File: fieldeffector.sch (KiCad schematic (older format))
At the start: 30 parts, among them J1 Conn_01x02, J10 Conn_01x02, J2 Conn_01x02, J3 Conn_01x02, J4 Conn_01x02, J5 Conn_01x02, J6 Conn_01x02, J7 Conn_01x02, J8 Conn_01x02, J9 Conn_01x02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

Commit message: update layout
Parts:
- added H1, H2, H3, H4: MountingHole, MountingHole:MountingHole_3.2mm_M3, symbol Mechanical:MountingHole
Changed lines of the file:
@@
 EESchema Schematic File Version 4
-LIBS:fieldeffect4-cache
+LIBS:fieldeffector-cache
 EELAYER 26 0
 EELAYER END
@@
 Wire Wire Line
 	7000 3000 7000 3050
+$Comp
+L Mechanical:MountingHole H3
+U 1 1 5CB01E0B
+P 1800 3400
+F 0 "H3" H 1900 3446 50  0000 L CNN
+F 1 "MountingHole" H 1900 3355 50  0000 L CNN
+F 2 "MountingHole:MountingHole_3.2mm_M3" H 1800 3400 50  0001 C CNN
+F 3 "~" H 1800 3400 50  0001 C CNN
+	1    1800 3400
+	1    0    0    -1
+$EndComp
+$Comp
+L Mechanical:MountingHole H4
+U 1 1 5CB023E2
+P 1800 3100
+F 0 "H4" H 1900 3146 50  0000 L CNN
+F 1 "MountingHole" H 1900 3055 50  0000 L CNN
+F 2 "MountingHole:MountingHole_3.2mm_M3" H 1800 3100 50  0001 C CNN
+F 3 "~" H 1800 3100 50  0001 C CNN
+	1    1800 3100
+	1    0    0    -1
+$EndComp
+$Comp
+L Mechanical:MountingHole H2
+U 1 1 5CB07684
+P 1450 3400
+F 0 "H2" H 1550 3446 50  0000 L CNN
+F 1 "MountingHole" H 1550 3355 50  0000 L CNN
+F 2 "MountingHole:MountingHole_3.2mm_M3" H 1450 3400 50  0001 C CNN
+F 3 "~" H 1450 3400 50  0001 C CNN
+	1    1450 3400
+	1    0    0    -1
+$EndComp
+$Comp
+L Mechanical:MountingHole H1
+U 1 1 5CB1AA81
+P 1450 3100
+F 0 "H1" H 1550 3146 50  0000 L CNN
+F 1 "MountingHole" H 1550 3055 50  0000 L CNN
+F 2 "MountingHole:MountingHole_3.2mm_M3" H 1450 3100 50  0001 C CNN
+F 3 "~" H 1450 3100 50  0001 C CNN
+	1    1450 3100
+	1    0    0    -1
+$EndComp
 $EndSCHEMATC

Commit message: add system ground
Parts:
- removed H3: MountingHole, MountingHole:MountingHole_3.2mm_M3, symbol Mechanical:MountingHole
- added H3: MountingHole_Pad, MountingHole:MountingHole_3.2mm_M3_Pad_Via, symbol Mechanical:MountingHole_Pad
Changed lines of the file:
@@
 	7000 3000 7000 3050
-$Comp
-L Mechanical:MountingHole H3
-U 1 1 5CB01E0B
-P 1800 3400
-F 0 "H3" H 1900 3446 50  0000 L CNN
-F 1 "MountingHole" H 1900 3355 50  0000 L CNN
-F 2 "MountingHole:MountingHole_3.2mm_M3" H 1800 3400 50  0001 C CNN
-F 3 "~" H 1800 3400 50  0001 C CNN
-	1    1800 3400
-	1    0    0    -1
-$EndComp
 $Comp
 L Mechanical:MountingHole H4
@@
 	1    0    0    -1
 $EndComp
+$Comp
+L Mechanical:MountingHole_Pad H3
+U 1 1 5CBA744D
+P 1800 3450
+F 0 "H3" H 1900 3501 50  0000 L CNN
+F 1 "MountingHole_Pad" H 1900 3410 50  0000 L CNN
+F 2 "MountingHole:MountingHole_3.2mm_M3_Pad_Via" H 1800 3450 50  0001 C CNN
+F 3 "~" H 1800 3450 50  0001 C CNN
+	1    1800 3450
+	1    0    0    -1
+$EndComp

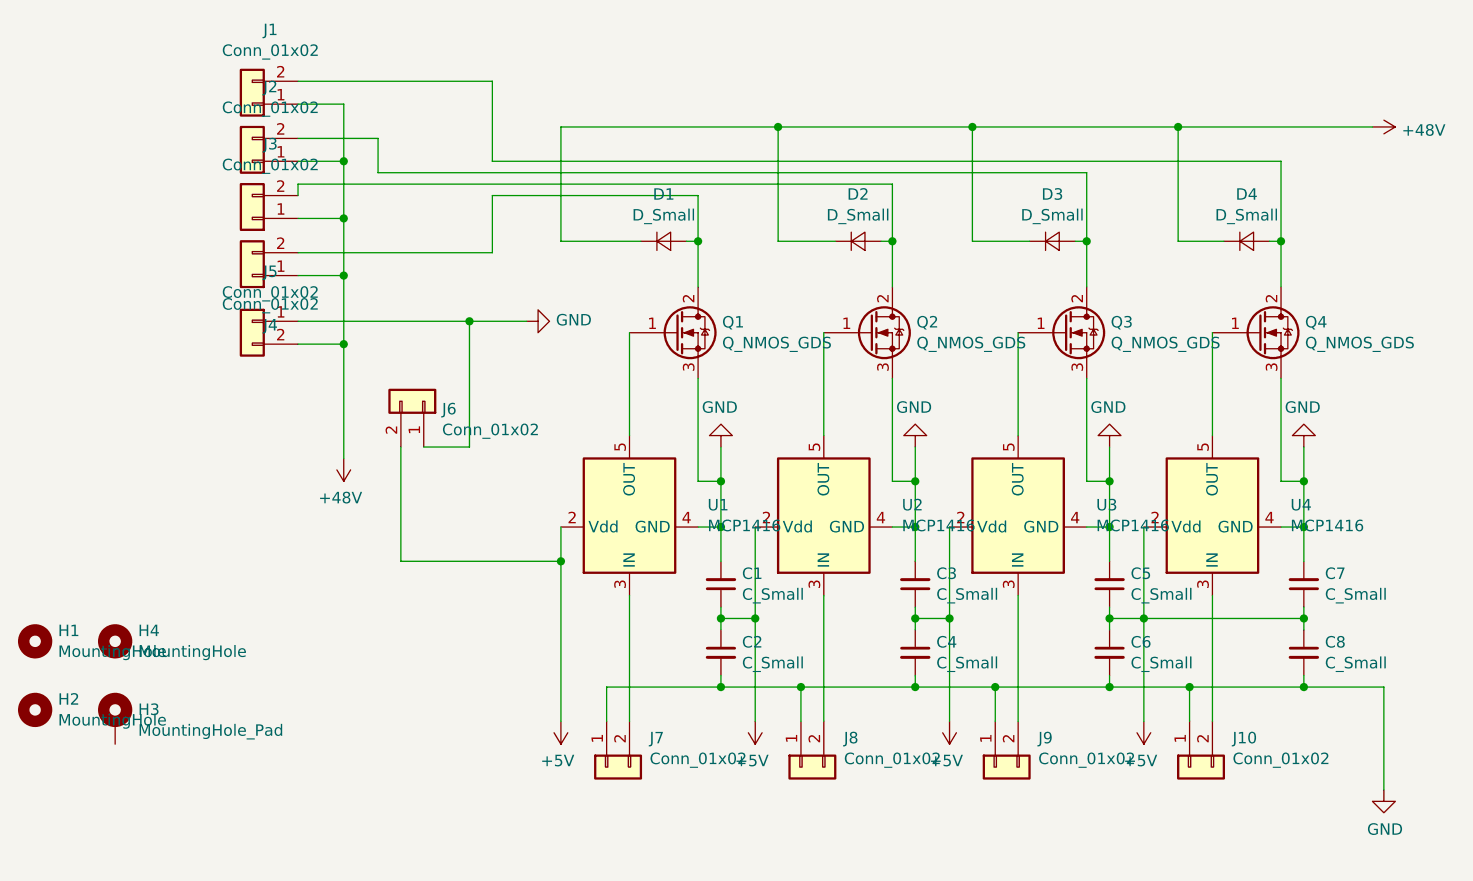
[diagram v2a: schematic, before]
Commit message: fixed diode pads
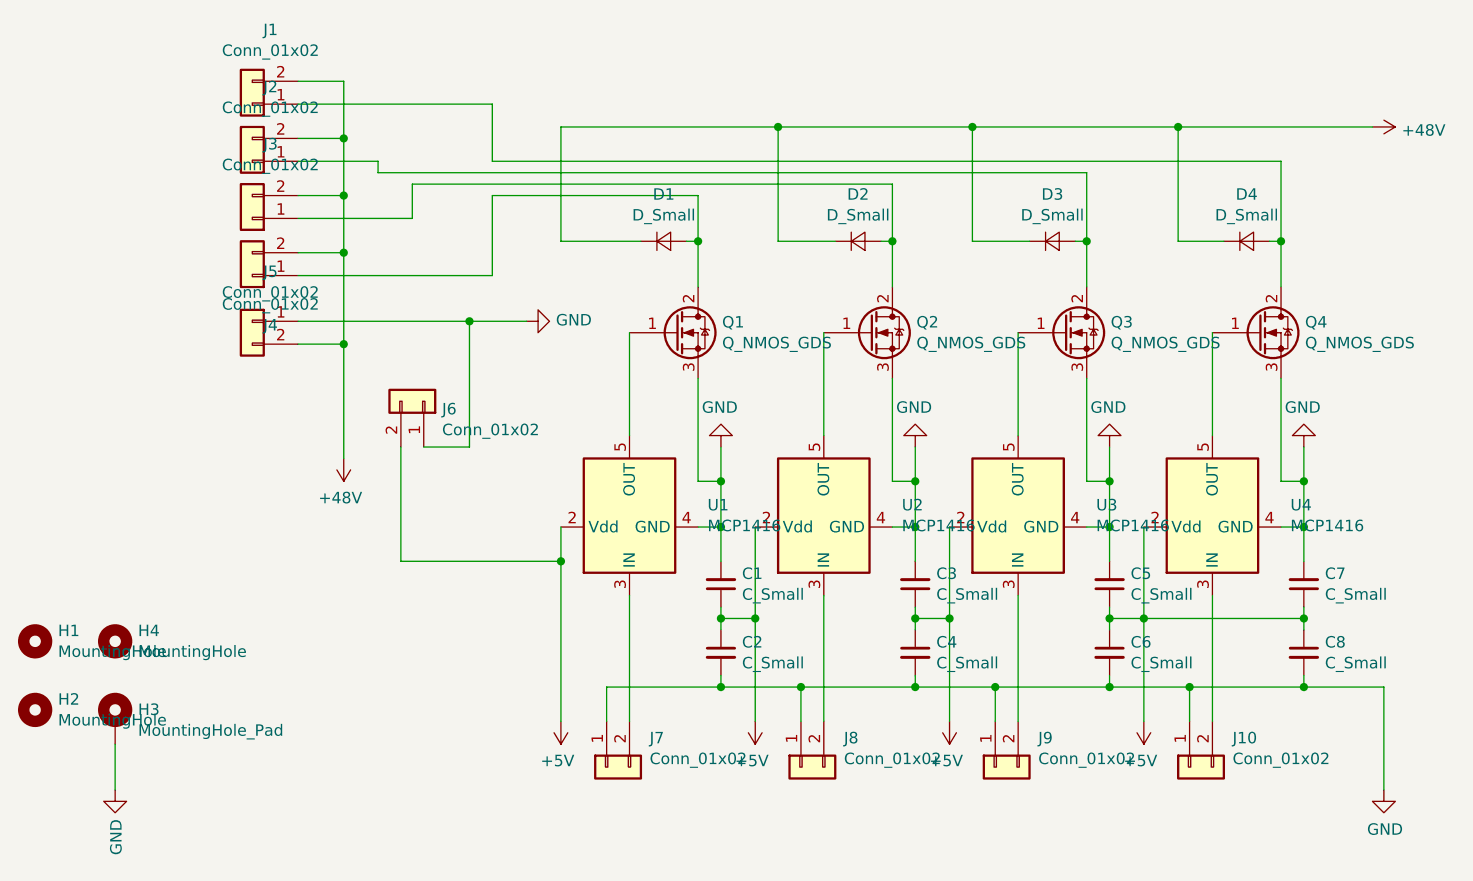
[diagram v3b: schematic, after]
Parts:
- D1, D2, D3, D4: footprint Diode_SMD:D_SOD-123F -> Diode_SMD:D_SMB
- J1, J2, J3, J4, J5: footprint Sockets_MOLEX_KK-System:Socket_MOLEX-KK-RM3-96mm_Lock_2pin_straight -> TerminalBlock_Phoenix:TerminalBlock_Phoenix_PT-1,5-2-3.5-H_1x02_P3.50mm_Horizontal
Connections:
- net +48V: now also J1.2 (Pin_2), J2.2 (Pin_2), J3.2 (Pin_2), J4.2 (Pin_2); no longer J1.1 (Pin_1), J2.1 (Pin_1), J3.1 (Pin_1), J4.1 (Pin_1)
- net GND: now also H3.1
- net at D1.2 (A), Q1.2 (D): now also J4.1 (Pin_1); no longer J4.2 (Pin_2)
- net at D2.2 (A), Q2.2 (D): now also J3.1 (Pin_1); no longer J3.2 (Pin_2)
- net at D3.2 (A), Q3.2 (D): now also J2.1 (Pin_1); no longer J2.2 (Pin_2)
- net at D4.2 (A), Q4.2 (D): now also J1.1 (Pin_1); no longer J1.2 (Pin_2)
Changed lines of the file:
@@
 EESchema Schematic File Version 4
 LIBS:fieldeffector-cache
-EELAYER 26 0
+EELAYER 29 0
 EELAYER END
 $Descr A4 11693 8268
@@
 F 0 "D1" H 4200 1555 50  0000 C CNN
 F 1 "D_Small" H 4200 1464 50  0000 C CNN
-F 2 "Diode_SMD:D_SOD-123F" V 4200 1350 50  0001 C CNN
+F 2 "Diode_SMD:D_SMB" V 4200 1350 50  0001 C CNN
 F 3 "~" V 4200 1350 50  0001 C CNN
 	1    4200 1350
@@
 F 0 "D2" H 5050 1555 50  0000 C CNN
 F 1 "D_Small" H 5050 1464 50  0000 C CNN
-F 2 "Diode_SMD:D_SOD-123F" V 5050 1350 50  0001 C CNN
+F 2 "Diode_SMD:D_SMB" V 5050 1350 50  0001 C CNN
 F 3 "~" V 5050 1350 50  0001 C CNN
 	1    5050 1350
@@
 F 0 "D3" H 5900 1555 50  0000 C CNN
 F 1 "D_Small" H 5900 1464 50  0000 C CNN
-F 2 "Diode_SMD:D_SOD-123F" V 5900 1350 50  0001 C CNN
+F 2 "Diode_SMD:D_SMB" V 5900 1350 50  0001 C CNN
 F 3 "~" V 5900 1350 50  0001 C CNN
 	1    5900 1350
@@
 F 0 "D4" H 6750 1555 50  0000 C CNN
 F 1 "D_Small" H 6750 1464 50  0000 C CNN
-F 2 "Diode_SMD:D_SOD-123F" V 6750 1350 50  0001 C CNN
+F 2 "Diode_SMD:D_SMB" V 6750 1350 50  0001 C CNN
 F 3 "~" V 6750 1350 50  0001 C CNN
 	1    6750 1350
@@
 F 0 "J2" H 2320 675 50  0000 C CNN
 F 1 "Conn_01x02" H 2320 766 50  0000 C CNN
-F 2 "Sockets_MOLEX_KK-System:Socket_MOLEX-KK-RM3-96mm_Lock_2pin_straight" H 2400 1000 50  0001 C CNN
+F 2 "TerminalBlock_Phoenix:TerminalBlock_Phoenix_PT-1,5-2-3.5-H_1x02_P3.50mm_Horizontal" H 2400 1000 50  0001 C CNN
 F 3 "~" H 2400 1000 50  0001 C CNN
 	1    2400 1000
@@
 F 0 "J3" H 2320 925 50  0000 C CNN
 F 1 "Conn_01x02" H 2320 1016 50  0000 C CNN
-F 2 "Sockets_MOLEX_KK-System:Socket_MOLEX-KK-RM3-96mm_Lock_2pin_straight" H 2400 1250 50  0001 C CNN
+F 2 "TerminalBlock_Phoenix:TerminalBlock_Phoenix_PT-1,5-2-3.5-H_1x02_P3.50mm_Horizontal" H 2400 1250 50  0001 C CNN
 F 3 "~" H 2400 1250 50  0001 C CNN
 	1    2400 1250
@@
 F 0 "J1" H 2320 425 50  0000 C CNN
 F 1 "Conn_01x02" H 2320 516 50  0000 C CNN
-F 2 "Sockets_MOLEX_KK-System:Socket_MOLEX-KK-RM3-96mm_Lock_2pin_straight" H 2400 750 50  0001 C CNN
+F 2 "TerminalBlock_Phoenix:TerminalBlock_Phoenix_PT-1,5-2-3.5-H_1x02_P3.50mm_Horizontal" H 2400 750 50  0001 C CNN
 F 3 "~" H 2400 750 50  0001 C CNN
 	1    2400 750
@@
 $EndComp
 Wire Wire Line
-	3450 1000 3450 650
-Wire Wire Line
-	3450 650  2600 650
-Wire Wire Line
-	2950 1050 2950 900
-Wire Wire Line
-	2950 900  2600 900
-Wire Wire Line
-	2950 1050 6050 1050
-Wire Wire Line
-	2600 1100 2600 1150
-Wire Wire Line
-	2600 1100 5200 1100
-Wire Wire Line
-	3450 1400 3450 1150
-Wire Wire Line
-	2800 750  2800 1000
-Wire Wire Line
-	2600 1000 2800 1000
-Connection ~ 2800 1000
-Wire Wire Line
-	2800 1000 2800 1250
-Wire Wire Line
-	2600 750  2800 750
-Wire Wire Line
-	2600 1250 2800 1250
-Connection ~ 2800 1250
+	3450 1000 3450 750
 $Comp
 L power:+48V #PWR0114
@@
 	1    0    0    -1
 $EndComp
-Wire Wire Line
-	2800 1250 2800 1500
-Wire Wire Line
-	2600 1500 2800 1500
-Connection ~ 2800 1500
-Wire Wire Line
-	2800 1500 2800 1800
-$Comp
-L Connector_Generic:Conn_01x02 J5
-U 1 1 5CC59094
-P 2400 1700
-F 0 "J5" H 2320 1917 50  0000 C CNN
-F 1 "Conn_01x02" H 2320 1826 50  0000 C CNN
-F 2 "Sockets_MOLEX_KK-System:Socket_MOLEX-KK-RM3-96mm_Lock_2pin_straight" H 2400 1700 50  0001 C CNN
-F 3 "~" H 2400 1700 50  0001 C CNN
-	1    2400 1700
-	-1   0    0    -1
-$EndComp
-Connection ~ 2800 1800
-Wire Wire Line
-	2800 1800 2800 2300
-Wire Wire Line
-	2600 1800 2800 1800
-Wire Wire Line
-	2600 1700 3350 1700
 $Comp
 L power:GND #PWR0116
@@
 	3150 2250 3350 2250
 Wire Wire Line
-	3350 2250 3350 1700
-Connection ~ 3350 1700
-Wire Wire Line
 	3350 1700 3600 1700
 Wire Wire Line
@@
 Wire Wire Line
 	3750 2750 3750 3450
-$Comp
-L Connector_Generic:Conn_01x02 J4
-U 1 1 5CB2EA20
-P 2400 1500
-F 0 "J4" H 2320 1717 50  0000 C CNN
-F 1 "Conn_01x02" H 2320 1626 50  0000 C CNN
-F 2 "Sockets_MOLEX_KK-System:Socket_MOLEX-KK-RM3-96mm_Lock_2pin_straight" H 2400 1500 50  0001 C CNN
-F 3 "~" H 2400 1500 50  0001 C CNN
-	1    2400 1500
-	-1   0    0    1
-$EndComp
-Wire Wire Line
-	2600 1400 3450 1400
 Wire Wire Line
 	4450 3250 4450 3300
@@
 	1    0    0    -1
 $EndComp
+Connection ~ 2800 1400
+Wire Wire Line
+	2600 1150 2800 1150
+Connection ~ 2800 1150
+Wire Wire Line
+	2800 1150 2800 1400
+Wire Wire Line
+	2600 900  2800 900
+Connection ~ 2800 900
+Wire Wire Line
+	2800 900  2800 1150
+Wire Wire Line
+	2800 650  2600 650
+Wire Wire Line
+	2800 650  2800 900
+Wire Wire Line
+	2600 750  3450 750
+Wire Wire Line
+	2600 1000 2950 1000
+Wire Wire Line
+	2950 1000 2950 1050
+Wire Wire Line
+	2600 1400 2800 1400
+$Comp
+L Connector_Generic:Conn_01x02 J4
+U 1 1 5CB2EA20
+P 2400 1500
+F 0 "J4" H 2320 1717 50  0000 C CNN
+F 1 "Conn_01x02" H 2320 1626 50  0000 C CNN
+F 2 "TerminalBlock_Phoenix:TerminalBlock_Phoenix_PT-1,5-2-3.5-H_1x02_P3.50mm_Horizontal" H 2400 1500 50  0001 C CNN
+F 3 "~" H 2400 1500 50  0001 C CNN
+	1    2400 1500
+	-1   0    0    1
+$EndComp
+Wire Wire Line
+	2950 1050 6050 1050
+Wire Wire Line
+	2600 1250 3100 1250
+Wire Wire Line
+	3100 1250 3100 1100
+Wire Wire Line
+	3100 1100 5200 1100
+Wire Wire Line
+	2600 1500 3450 1500
+Wire Wire Line
+	3450 1150 3450 1500
+Wire Wire Line
+	3350 1700 3350 2250
+Wire Wire Line
+	2800 1400 2800 1800
+Connection ~ 2800 1800
+Wire Wire Line
+	2800 1800 2800 2300
+Wire Wire Line
+	2600 1800 2800 1800
+$Comp
+L Connector_Generic:Conn_01x02 J5
+U 1 1 5CC59094
+P 2400 1700
+F 0 "J5" H 2320 1917 50  0000 C CNN
+F 1 "Conn_01x02" H 2320 1826 50  0000 C CNN
+F 2 "TerminalBlock_Phoenix:TerminalBlock_Phoenix_PT-1,5-2-3.5-H_1x02_P3.50mm_Horizontal" H 2400 1700 50  0001 C CNN
+F 3 "~" H 2400 1700 50  0001 C CNN
+	1    2400 1700
+	-1   0    0    -1
+$EndComp
+Wire Wire Line
+	2600 1700 3350 1700
+Connection ~ 3350 1700
+Wire Wire Line
+	1800 3550 1800 3750
+$Comp
+L power:GND #PWR?
+U 1 1 5D02EA66
+P 1800 3750
+F 0 "#PWR?" H 1800 3500 50  0001 C CNN
+F 1 "GND" V 1805 3622 50  0000 R CNN
+F 2 "" H 1800 3750 50  0001 C CNN
+F 3 "" H 1800 3750 50  0001 C CNN
+	1    1800 3750
+	1    0    0    -1
+$EndComp
